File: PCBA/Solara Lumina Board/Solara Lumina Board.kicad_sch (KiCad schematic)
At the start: 0 parts

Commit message: Added ESP32-C6 and increased board size
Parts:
- added U1: ESP32-C6-WROOM-1-N8, ClementsFootprints:ESP32-C6-WROOM-1-N8, symbol clement-components:MCUs/ESP32-C6-WROOM-1-N8
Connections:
- new net: U1.29_1 (GND), U1.29_2 (GND), U1.29_3 (GND), U1.29_4 (GND), U1.29_5 (GND)
- new net: U1.29_6 (GND), U1.29_7 (GND), U1.29_8 (GND), U1.29_9 (GND)

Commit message: Adding parts!
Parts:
- added D1: TEMD6200FX01, ClementsFootprints:PhotoDiode-0805, symbol clement-components:Diodes/TEMD6200FX01
- added TH1: P0K1.520.6W.A.010, Connector_PinHeader_2.00mm:PinHeader_1x02_P2.00mm_Vertical, symbol clement-components:Sensors/P0K1.520.6W.A.010
- added U2: LM5169FDDAR, Package_SO:TI_SO-PowerPAD-8, symbol clement-components:PMICs/LM5169FDDAR
- added U3: ADS1015IDGS, Package_SO:TSSOP-10_3x3mm_P0.5mm, symbol Analog_ADC:ADS1015IDGS

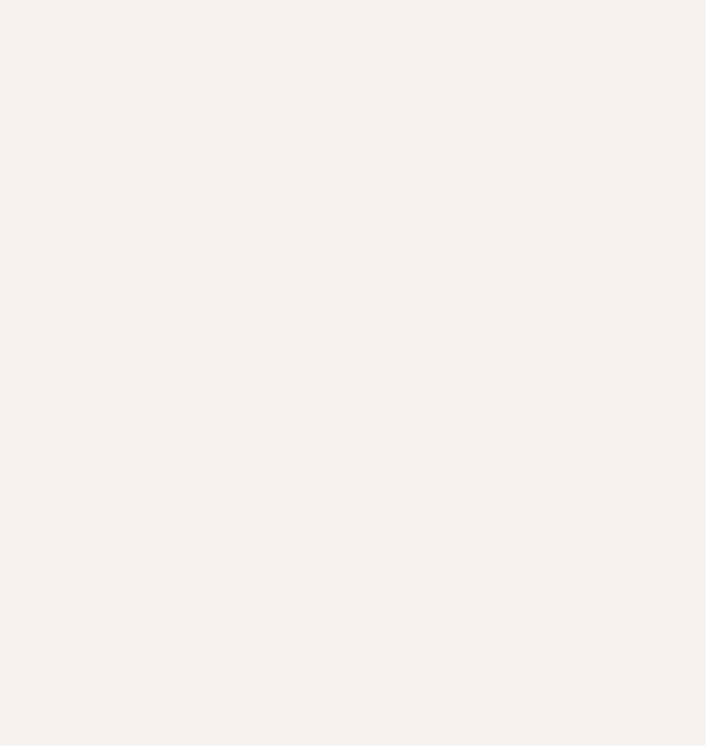
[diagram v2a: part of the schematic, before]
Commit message: Added the op-amp eek
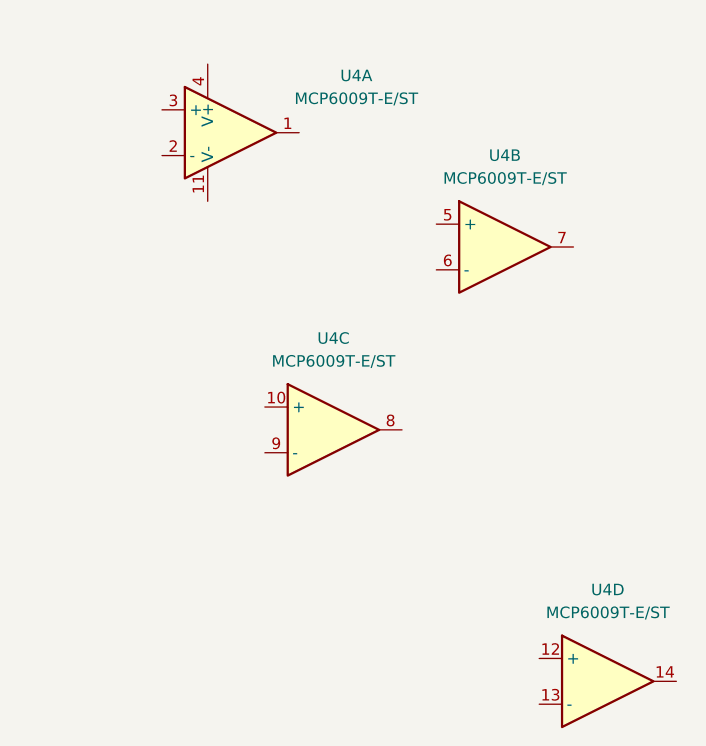
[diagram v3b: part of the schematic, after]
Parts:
- added U4: MCP6009T-E/ST, Package_SO:TSSOP-14_4.4x5mm_P0.65mm, symbol clement-components:Op Amps/MCP6009T-E/ST

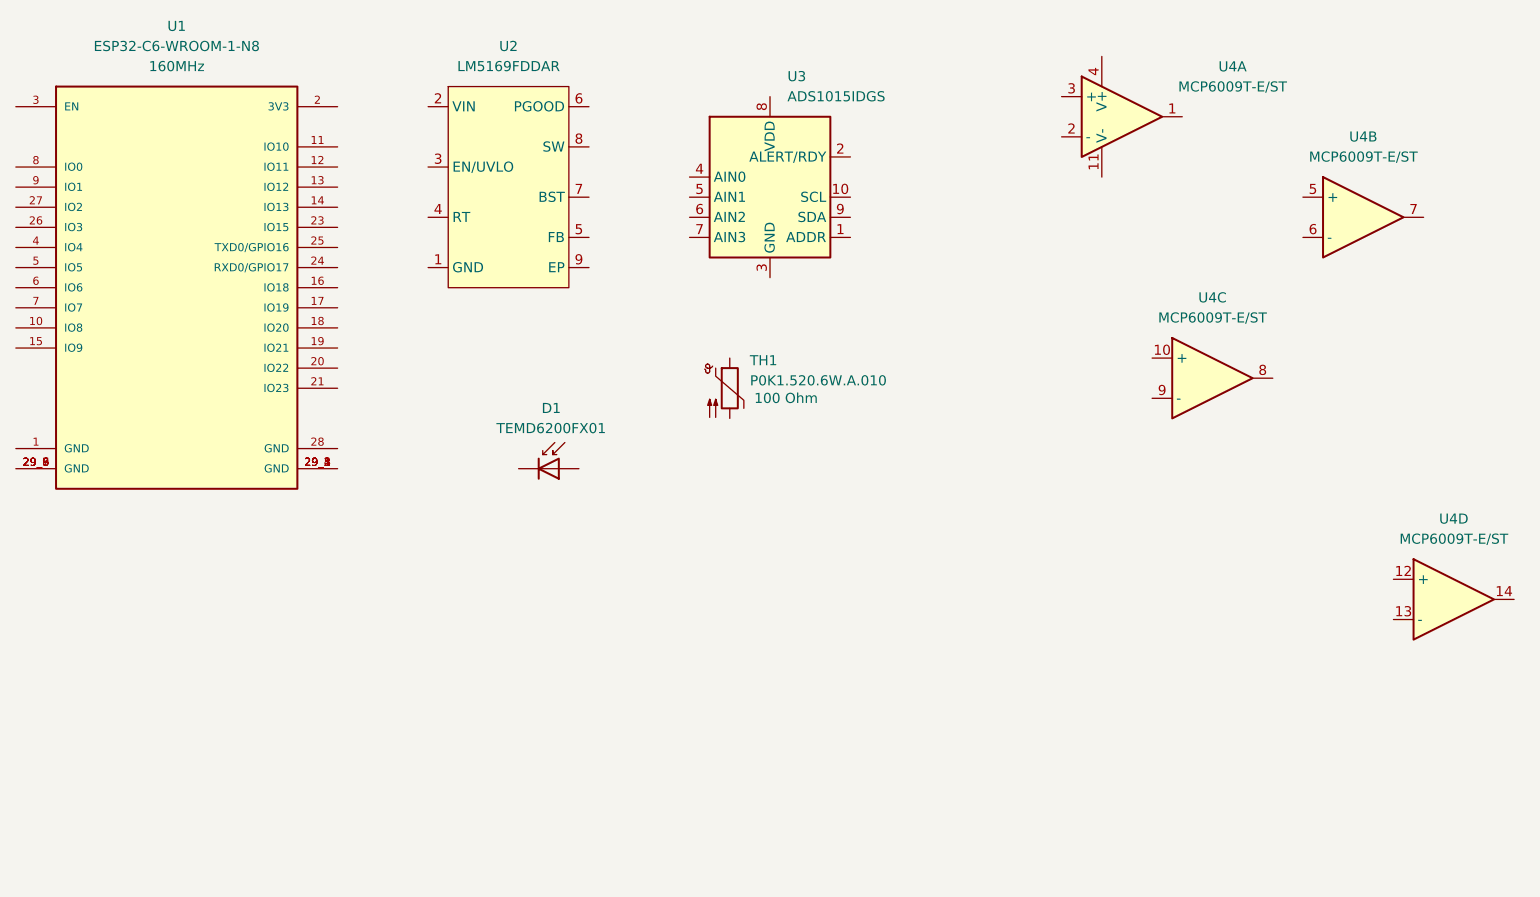
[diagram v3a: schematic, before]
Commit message: Added more parts and adjusted board outline
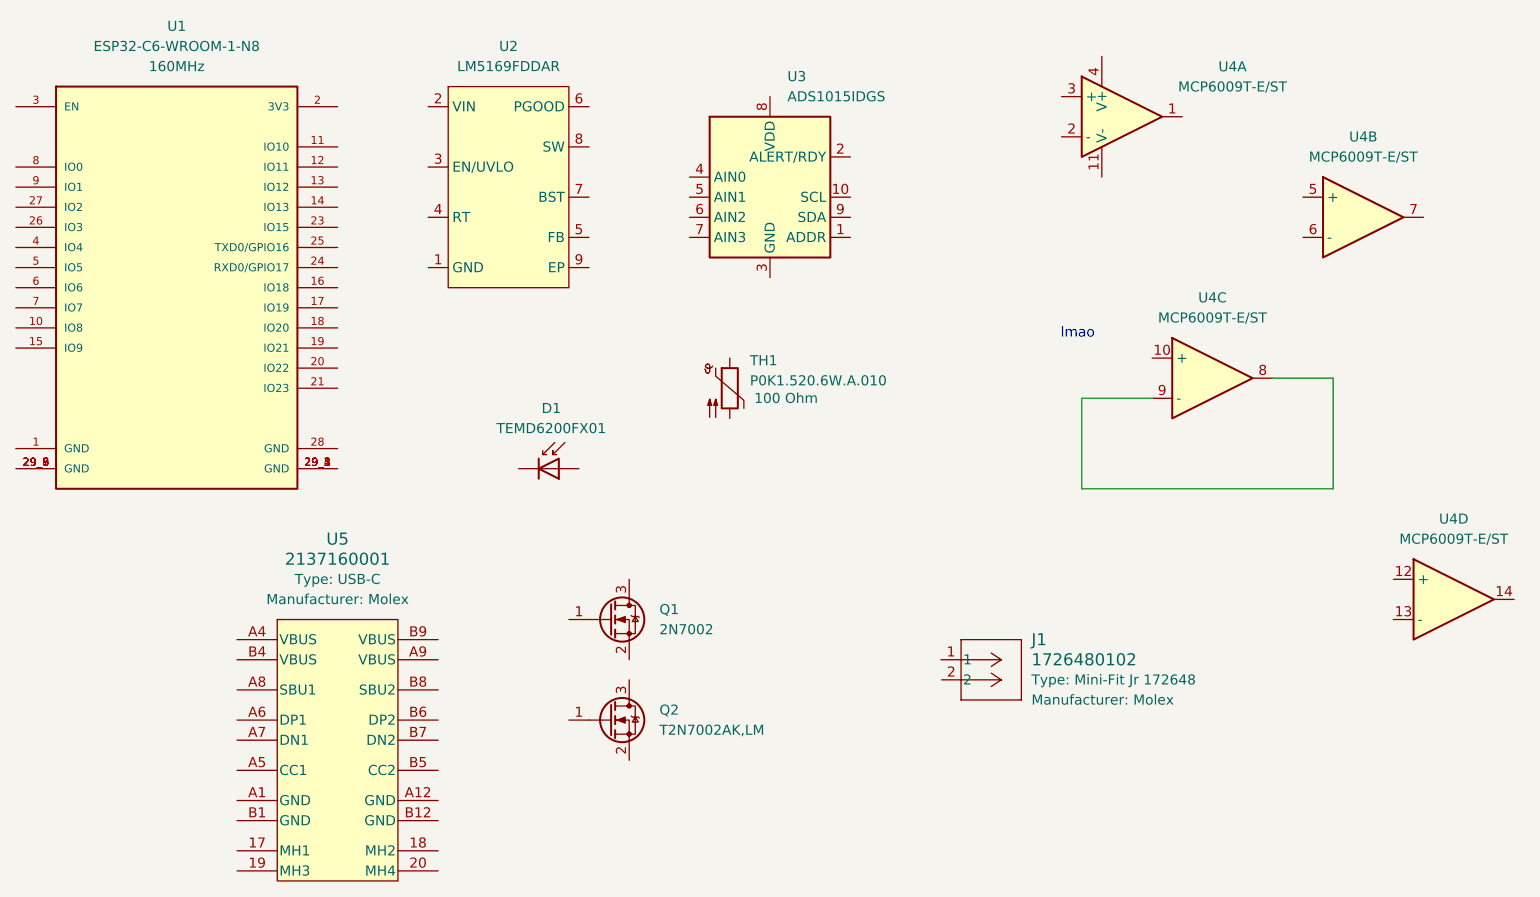
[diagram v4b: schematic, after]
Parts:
- added J1: 1726480102, ClementsFootprints:Molex_1726480102, symbol clement-components:Connectors/1726480102
- added Q1: 2N7002, Package_TO_SOT_SMD:SOT-23, symbol Transistor_FET:2N7002
- added Q2: T2N7002AK,LM, Package_TO_SOT_SMD:SOT-23, symbol clement-components:MOSFETs/T2N7002AK,LM
- added U5: 2137160001, ClementsFootprints:USB-C-2137160001, symbol clement-components:Connectors/2137160001
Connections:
- net at U4.8: now also U4.9 (-)
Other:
- note added: "lmao"
